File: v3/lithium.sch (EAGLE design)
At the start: 60 parts, among them J1 batt, J2 battery, J3 motor, J4 AVR_ISP, Q1 Si7137DP, Q1_R1 100k, U1 TPS61088VQFN20, U1_C22 8.2nF, U1_CBST 100nF, U1_CCOMP 680PF, U1_CCOMP2 36pF, U1_CIN 0.47uF, U1_CIN2 100nF, U1_COUT 0.47uF, U1_CVCC 1uF, U1_L1 DR73-1R0-R, U1_RCOMP 38.3K Ohms, U1_RFBB 118K Ohms, U1_RFBT 470K Ohms, U1_RLIM 102K Ohms, U1_RT 261K Ohms, U2 ATTINY84-20MU, U2_C1 10nF, U2_C2 2.2uF, U2_R1 10k, U2_R2 10k, U4 TPS2113APWR, U4_C3 0.1uF, U4_C4 0.1uF, U4_RPG 100K Ohms, U5 MCP73833-FCI/UN, U5_C1 1.0uF, U5_C2 1.0uF, U5_R1 1K Ohm, U6 TPS61230A, U6_CBST 10 nF, U6_CFF 10pF, U6_CIN 22uF, U6_COUT 22uF, U6_RFBB 100K Ohms, U6_RFBT 316K Ohms

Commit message: Some small, post-rev0 tweaks.
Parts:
- R1, R3, R5: value 15 Ohm -> 150 Ohm; device Vishay_By_element14_Batch_1:CRCW080515R0JNEA -> Panasonic_By_element14_Batch_1:ERA-6AEB151V
- R2: value 15 Ohm -> 200 Ohm; device Vishay_By_element14_Batch_1:CRCW080515R0JNEA -> Panasonic_By_element14_Batch_1:ERA-6AEB201V
- R4, R6: value 15 Ohm -> 100 Ohm; device Vishay_By_element14_Batch_1:CRCW080515R0JNEA -> Panasonic_By_element14_Batch_1:ERA-6AEB101V
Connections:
- net LA_5: now also R1.R1; no longer R1.1
- net LA_6: now also R2.R1; no longer R2.1
- net LA_BATT: now also R6.R1; no longer R6.1
- net LA_CHG: now also R3.R1; no longer R3.1
- net LA_DONE: now also R4.R1; no longer R4.1
- net LA_USB: now also R5.R1; no longer R5.1
- net MOT_6V: now also R2.R2; no longer R2.2
- net SYS_5V: now also R1.R2; no longer R1.2
- net VCC: now also R6.R2; no longer R6.2
- net VUSB: now also R3.R2, R4.R2, R5.R2; no longer R3.2, R4.2, R5.2
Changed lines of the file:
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@@
 <part name="U6_COUT" library="Murata_By_element14_Batch_1" deviceset="GRM32ER61C226KE20L" device="" value="22uF"/>
 <part name="GND" library="SparkFun-PowerSymbols" deviceset="GND" device=""/>
-<part name="R1" library="Vishay_By_element14_Batch_1" deviceset="CRCW080515R0JNEA" device="" value="15 Ohm"/>
-<part name="R2" library="Vishay_By_element14_Batch_1" deviceset="CRCW080515R0JNEA" device="" value="15 Ohm"/>
-<part name="R3" library="Vishay_By_element14_Batch_1" deviceset="CRCW080515R0JNEA" device="" value="15 Ohm"/>
-<part name="R4" library="Vishay_By_element14_Batch_1" deviceset="CRCW080515R0JNEA" device="" value="15 Ohm"/>
-<part name="R5" library="Vishay_By_element14_Batch_1" deviceset="CRCW080515R0JNEA" device="" value="15 Ohm"/>
-<part name="R6" library="Vishay_By_element14_Batch_1" deviceset="CRCW080515R0JNEA" device="" value="15 Ohm"/>
+<part name="R1" library="Panasonic_By_element14_Batch_1" deviceset="ERA-6AEB151V" device="" value="150 Ohm"/>
+<part name="R2" library="Panasonic_By_element14_Batch_1" deviceset="ERA-6AEB201V" device="" value="200 Ohm"/>
+<part name="R3" library="Panasonic_By_element14_Batch_1" deviceset="ERA-6AEB151V" device="" value="150 Ohm"/>
+<part name="R4" library="Panasonic_By_element14_Batch_1" deviceset="ERA-6AEB101V" device="" value="100 Ohm"/>
+<part name="R5" library="Panasonic_By_element14_Batch_1" deviceset="ERA-6AEB151V" device="" value="150 Ohm"/>
+<part name="R6" library="Panasonic_By_element14_Batch_1" deviceset="ERA-6AEB101V" device="" value="100 Ohm"/>
 <part name="R7" library="Vishay_By_element14_Batch_1" deviceset="CRCW040222R0JNED" device="" value="22 Ohms"/>
 <part name="J1" library="SparkFun-Connectors" deviceset="CONN_02" device="-JST-2MM-SMT" value="batt"/>
@@
 <wire x1="261.62" y1="119.38" x2="261.62" y2="127" width="0.1524" layer="91"/>
 <label x="262.89" y="124.968" size="1.778" layer="95"/>
-<pinref part="R6" gate="A" pin="2"/>
+<pinref part="R6" gate="A" pin="R2"/>
 </segment>
 <segment>
@@
 <pinref part="MOTORS" gate="A" pin="2"/>
 <wire x1="200.66" y1="101.6" x2="200.66" y2="106.68" width="0.1524" layer="91"/>
-<pinref part="R2" gate="A" pin="1"/>
+<pinref part="R2" gate="A" pin="R1"/>
 </segment>
 </net>
@@
 <pinref part="5V" gate="A" pin="2"/>
 <wire x1="185.42" y1="101.6" x2="185.42" y2="106.68" width="0.1524" layer="91"/>
-<pinref part="R1" gate="A" pin="1"/>
+<pinref part="R1" gate="A" pin="R1"/>
 </segment>
 </net>
@@
 <wire x1="200.66" y1="119.38" x2="200.66" y2="127" width="0.1524" layer="91"/>
 <label x="201.676" y="125.222" size="1.778" layer="95"/>
-<pinref part="R2" gate="A" pin="2"/>
+<pinref part="R2" gate="A" pin="R2"/>
 </segment>
 <segment>
@@
 <junction x="215.9" y="170.18"/>
 <label x="203.2" y="171.45" size="1.778" layer="95"/>
-<pinref part="R3" gate="A" pin="2"/>
-<pinref part="R4" gate="A" pin="2"/>
-<pinref part="R5" gate="A" pin="2"/>
+<pinref part="R3" gate="A" pin="R2"/>
+<pinref part="R4" gate="A" pin="R2"/>
+<pinref part="R5" gate="A" pin="R2"/>
 </segment>
 <segment>
@@
 <pinref part="CHG" gate="A" pin="2"/>
 <wire x1="215.9" y1="106.68" x2="215.9" y2="101.6" width="0.1524" layer="91"/>
-<pinref part="R3" gate="A" pin="1"/>
+<pinref part="R3" gate="A" pin="R1"/>
 </segment>
 </net>
@@
 <pinref part="DONE" gate="A" pin="2"/>
 <wire x1="231.14" y1="106.68" x2="231.14" y2="101.6" width="0.1524" layer="91"/>
-<pinref part="R4" gate="A" pin="1"/>
+<pinref part="R4" gate="A" pin="R1"/>
 </segment>
 </net>
@@
 <pinref part="USB" gate="A" pin="2"/>
 <wire x1="246.38" y1="101.6" x2="246.38" y2="106.68" width="0.1524" layer="91"/>
-<pinref part="R5" gate="A" pin="1"/>
+<pinref part="R5" gate="A" pin="R1"/>
 </segment>
 </net>
@@
 <pinref part="BATT" gate="A" pin="2"/>
 <wire x1="261.62" y1="106.68" x2="261.62" y2="101.6" width="0.1524" layer="91"/>
-<pinref part="R6" gate="A" pin="1"/>
+<pinref part="R6" gate="A" pin="R1"/>
 </segment>
 </net>
@@
 <wire x1="185.42" y1="119.38" x2="185.42" y2="127" width="0.1524" layer="91"/>
 <label x="186.436" y="125.222" size="1.778" layer="95"/>
-<pinref part="R1" gate="A" pin="2"/>
-</segment>
-<segment>
+<pinref part="R1" gate="A" pin="R2"/>
+</segment>
+<segment>

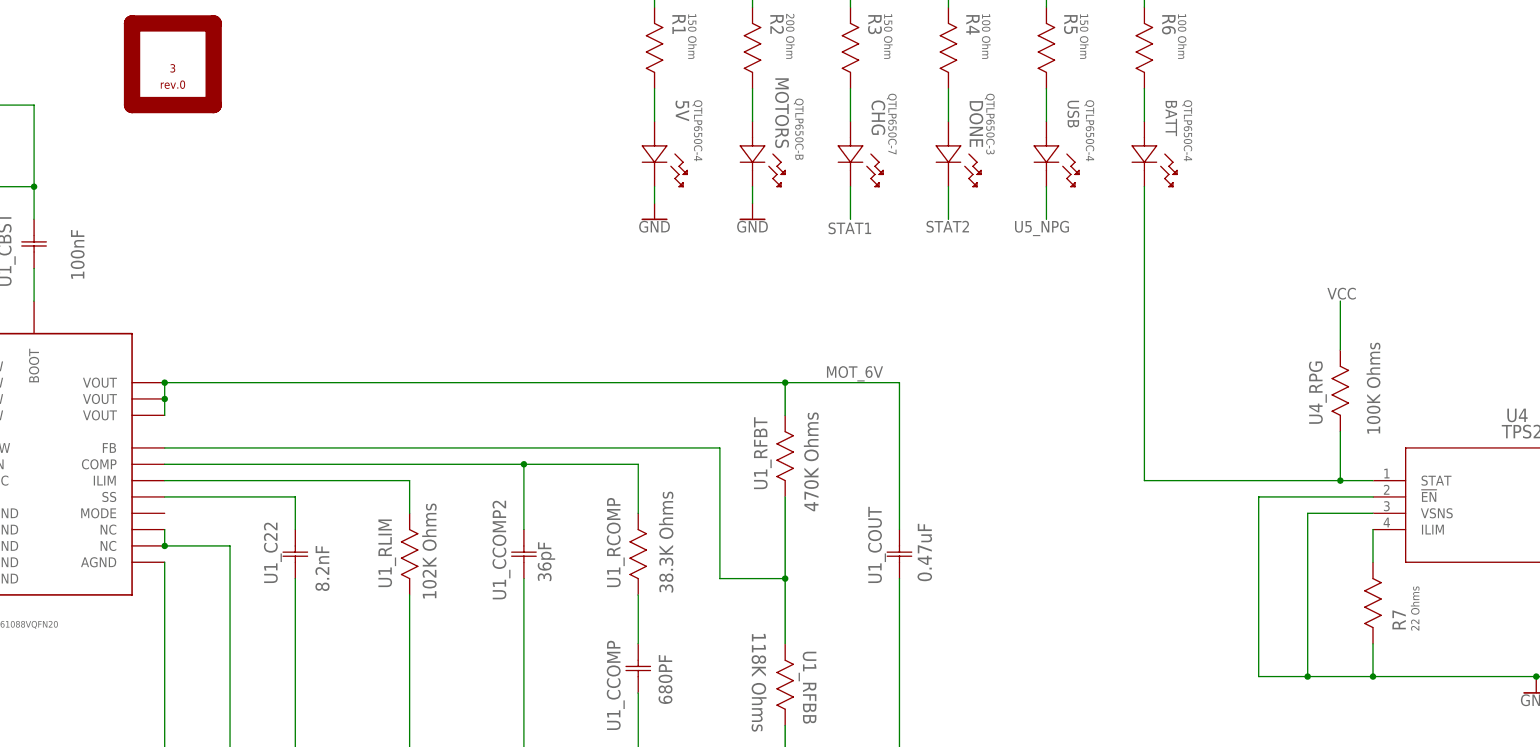
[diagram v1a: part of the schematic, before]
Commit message: Starting Boron evaluation of bq24160
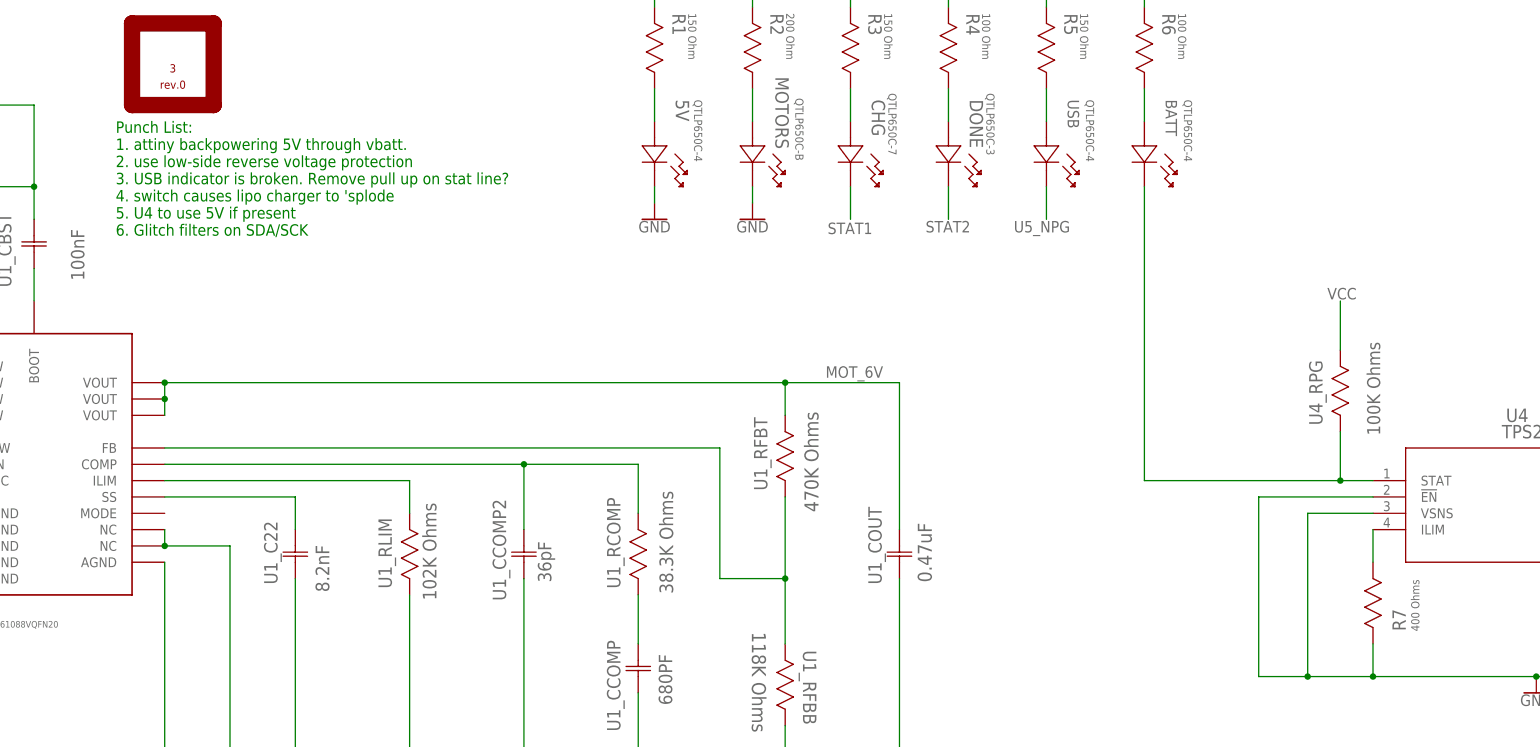
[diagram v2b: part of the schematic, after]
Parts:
- R7: value 22 Ohms -> 400 Ohms
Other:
- note added: "Punch List: 1. attiny backpowering 5V through vbatt. 2. use low-side reverse voltage protection 3. USB indicator is broken. Remove pull up on stat line? 4. switch causes lipo charger to 'splode 5. U4 to use 5V if present 6. Glitch filters on SDA/SCK"
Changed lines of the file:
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@@
 <part name="R5" library="Panasonic_By_element14_Batch_1" deviceset="ERA-6AEB151V" device="" value="150 Ohm"/>
 <part name="R6" library="Panasonic_By_element14_Batch_1" deviceset="ERA-6AEB101V" device="" value="100 Ohm"/>
-<part name="R7" library="Vishay_By_element14_Batch_1" deviceset="CRCW040222R0JNED" device="" value="22 Ohms"/>
+<part name="R7" library="Vishay_By_element14_Batch_1" deviceset="CRCW040222R0JNED" device="" value="400 Ohms"/>
 <part name="J1" library="SparkFun-Connectors" deviceset="CONN_02" device="-JST-2MM-SMT" value="batt"/>
 <part name="R8" library="Vishay_By_element14_Batch_1" deviceset="CRCW08050000Z0EB" device="" value="0Ohm"/>
@@
 <sheet>
 <plain>
+<text x="101.6" y="83.82" size="1.778" layer="91">Punch List:
+1. attiny backpowering 5V through vbatt.
+2. use low-side reverse voltage protection
+3. USB indicator is broken. Remove pull up on stat line?
+4. switch causes lipo charger to 'splode
+5. U4 to use 5V if present
+6. Glitch filters on SDA/SCK</text>
 </plain>
 <instances>
@@
 </schematic>
 </drawing>
+<compatibility>
+<note version="6.3" minversion="6.2.2" severity="warning">
+Since Version 6.2.2 text objects can contain more than one line,
+which will not be processed correctly with this version.
+</note>
+</compatibility>
 </eagle>

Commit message: Starting Rev 2 of Lithium.
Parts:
- removed D1: 1SS367,H3F, SparkFun-DiscreteSemi:DIODE-SCHOTTKY-BAT20J
- removed J4: AVR_ISP, 32bits:AVR_ISP
- removed Q1_R1: 100k, SparkFun-Resistors:100KOHM-0603-1/10W-1%
- removed R7: 400 Ohms, Vishay_By_element14_Batch_1:CRCW040222R0JNED
- removed R9: 10k, 32bits:NTHS1206N02N1002JE
- removed U2: ATTINY84-20MU, 32bits:ATTINY84-20MU
- removed U2_R1: 10k, SparkFun-Resistors:RESISTOR0402
- removed U4: TPS2113APWR, 32bits:TPS2113APWR
- removed U4_C3, U4_C4: 0.1uF, SparkFun-Capacitors:0.1UF-0402-16V-10%
- removed U4_RPG: 100K Ohms, Vishay_By_element14_Batch_1:CRCW1206100KFKEA
- removed U5: MCP73833-FCI/UN, 32bits:MCP73833-FCI/UN
- removed U5_C1, U5_C2: 1.0uF, SparkFun-Capacitors:1.0UF-0402-16V-10%
- removed U5_R1: 1K Ohm, Vishay_By_element14_Batch_1:CRCW04021K00JNED
- added J5: FTSH-105-01-XXX-DV-K, FTSH-105-01-XXX-DV-K:FTSH-105-01-XXX-DV-K
- added U3: MKL02Z8VFG4, 32bits:MKL02Z8VFG4
- added U7: BQ24168RGET, 32bits:BQ24168RGET
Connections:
- removed net !RESET: J4.!RESET, U2.PB3_(PCINT11/RESET!/DW)
- removed net MISO: J4.MISO, U2.PA5
- removed net Q1_GATE: D1.A, Q1.GATE, Q1_R1.2
- removed net S1_U4OUT: S1.P$1, U4.OUT
- removed net U4_ILIM: R7.1, U4.ILIM
- removed net U4_STAT: BATT.1, U4.STAT, U4_RPG.2
- removed net U5_PROG: U5.PROG, U5_R1.1
- removed net U5_THERM: R9.2, U5.THERM
- removed net VBAT: D1.C, Q1.SOURCE#1, Q1.SOURCE#2, Q1.SOURCE#3, U2.(ADC0/AREF/PCINT0)_PA0, U4.IN1, U4_C4.1, U5.VBAT, U5.VBAT_2, U5_C2.1
- net GND: no longer J4.GND, Q1_R1.1, R7.2, R9.1, U2.GND, U4.!EN, U4.GND, U4.VSNS, U4_C3.2, U4_C4.2, U5.VSS, U5_C1.2, U5_C2.2, U5_R1.2
- net MOSI/SDA: no longer J4.MOSI, U2.PA6, U2_R1.1
- net MOT_6V: no longer U2.(ADC1/AIN0/PCINT1)_PA1
- net SCK: now also U3.PTA3; no longer J4.SCK, U2.(ADC4/USCK/SCL/T1/PCINT4)_PA4
- net STAT1: no longer U5.STAT1
- net STAT2: no longer U5.STAT2
- net SYS_5V: no longer J4.VTG, U2.(ADC2/AIN1/PCINT2)_PA2, U2.VCC, U2_R1.2
- net U5_NPG: no longer U5.!PG
- net VBAT_CON: no longer Q1.DRAIN#5, Q1.DRAIN#6, Q1.DRAIN#7, Q1.DRAIN#8
- net VCC: no longer U4_RPG.1
- net VUSB: no longer U4.IN2, U4_C3.1, U5.VDD, U5.VDD_2, U5_C1.1
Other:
- note removed: "Punch List: 1. attiny backpowering 5V through vbatt. 2. use low-side reverse voltage protection 3. USB indicator is broken. Remove pull up on stat line? 4. switch causes lipo charger to 'splode 5. U4 to use 5V if present 6. Glitch filters on SDA/SCK"
- moved on the sheet: Q1

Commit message: Progress on Lithium rev 2
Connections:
- net GND: now also U3.VREFLVSS
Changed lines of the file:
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@@
 <part name="J5" library="FTSH-105-01-XXX-DV-K" deviceset="FTSH-105-01-XXX-DV-K" device=""/>
 <part name="U7" library="32bits" deviceset="BQ24168RGET" device=""/>
+<part name="GND4" library="SparkFun-PowerSymbols" deviceset="GND" device=""/>
 </parts>
 <sheets>
@@
 <instance part="J5" gate="G$1" x="-15.24" y="218.44"/>
 <instance part="U7" gate="A" x="294.64" y="48.26"/>
+<instance part="GND4" gate="1" x="30.48" y="-35.56"/>
 </instances>
 <busses>
@@
 <pinref part="U2_C2" gate="A" pin="C2"/>
 </segment>
+<segment>
+<pinref part="U3" gate="A" pin="VREFLVSS"/>
+<wire x1="48.26" y1="-43.18" x2="38.1" y2="-43.18" width="0.1524" layer="91"/>
+<wire x1="38.1" y1="-43.18" x2="38.1" y2="-30.48" width="0.1524" layer="91"/>
+<wire x1="38.1" y1="-30.48" x2="30.48" y2="-30.48" width="0.1524" layer="91"/>
+<wire x1="30.48" y1="-30.48" x2="30.48" y2="-33.02" width="0.1524" layer="91"/>
+<pinref part="GND4" gate="1" pin="GND"/>
+</segment>
 </net>
 <net name="SW" class="0">
@@
 <segment>
 <wire x1="12.7" y1="-45.72" x2="12.7" y2="-33.02" width="0.1524" layer="91"/>
-<label x="22.86" y="-37.846" size="1.778" layer="95"/>
+<label x="43.18" y="-45.466" size="1.778" layer="95"/>
 <pinref part="U2_R2" gate="G$1" pin="1"/>
 <pinref part="U3" gate="A" pin="PTA3"/>
